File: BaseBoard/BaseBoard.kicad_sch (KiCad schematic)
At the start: 47 parts, among them J1 USB_C_DEALON-USB-US31-106, J2 Serial Port, J3 add-on conn, Q1 PMN48XP, SW1 SW_DIP_x08, SW2 boot, SW3 Reset, U1 ESP32-WROOM-E, U2 4021, U3 MCP73831-2ACI-OT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

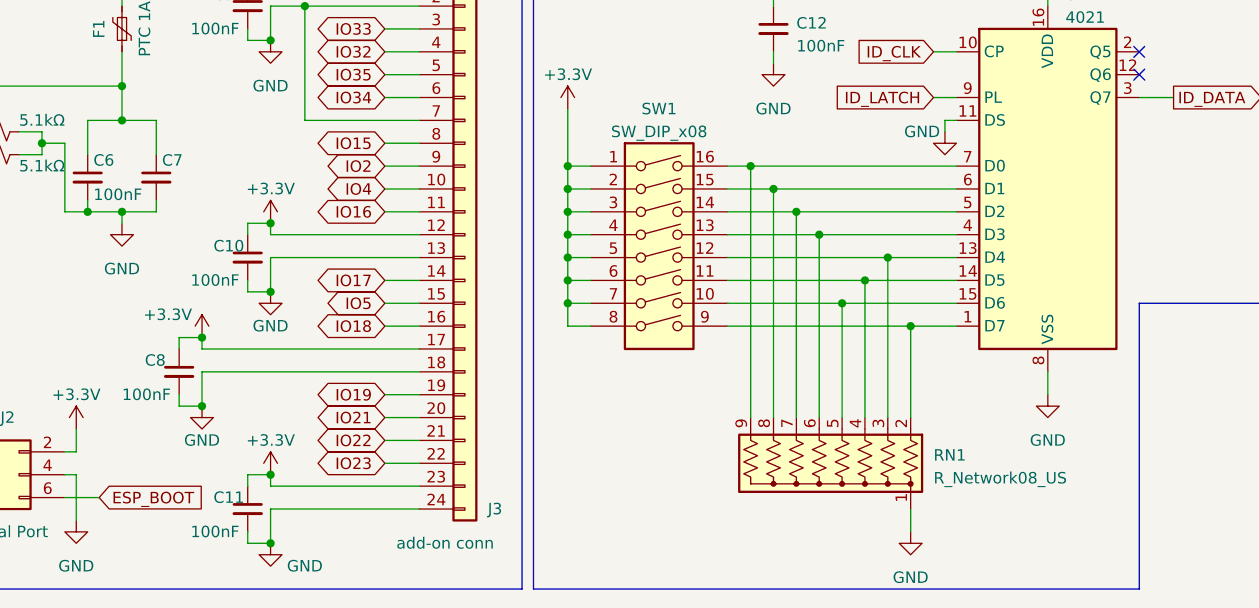
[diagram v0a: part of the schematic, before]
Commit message: Switches Resistor Network for actual footprint
We'll use the 746X101 which has a smaller footprint.
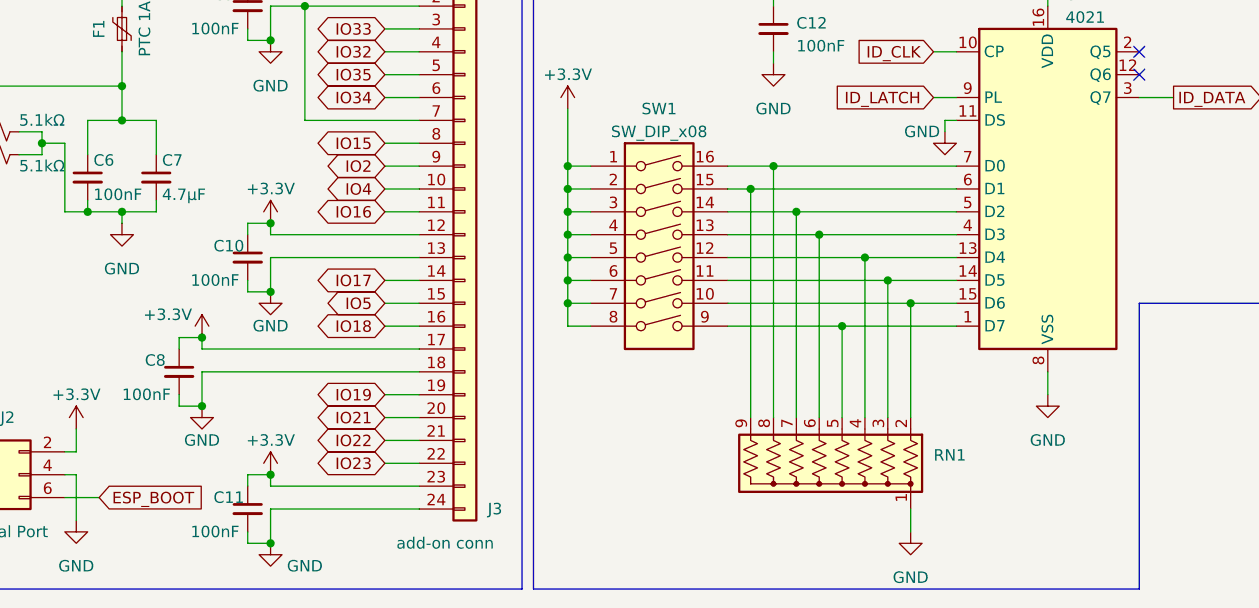
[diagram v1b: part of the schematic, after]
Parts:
- C7: value (none) -> 4.7µF
- RN1: value R_Network08_US -> (none); footprint Resistor_SMD:R_Array_Convex_5x1206 -> (none)
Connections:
- net at SW1.9, U2.1 (D7): now also RN1.5 (R4); no longer RN1.2 (R1)
- net at SW1.12, U2.13 (D4): now also RN1.4 (R3); no longer RN1.3 (R2)
- net at SW1.11, U2.14 (D5): now also RN1.3 (R2); no longer RN1.4 (R3)
- net at SW1.10, U2.15 (D6): now also RN1.2 (R1); no longer RN1.5 (R4)
- net at SW1.15, U2.6 (D1): now also RN1.9 (R8); no longer RN1.8 (R7)
- net at SW1.16, U2.7 (D0): now also RN1.8 (R7); no longer RN1.9 (R8)

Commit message: Moves symbol and footprint libraries to parent directory
This will allow us to use the symbols and footprints on other boards.
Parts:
- J3: value add-on conn -> (none)
- RN1: value (none) -> 10kΩ

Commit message: Fixes RGB led symbol
The Hongzhi Forest HS-1204-RGB is actually a BGAR led. Pin 1 is blue, 2
is green, 3 is the anode and 4 is red. The old symbol had red and the
anode swapped, which means the LED doesn't work correctly in rev 0.1 of
the board.
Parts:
- removed D2: LED_RGBA, GameOver:Hongzhi_Forest_HS-1204-RGB, symbol Device:LED_RGBA
- added D2: LED_BGAR, symbol Device:LED_BGAR
- J3: value (none) -> base connector
- RN1: footprint (none) -> GameOver:746X101
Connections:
- net +3V3: now also D2.3 (A)
- net at R12.2: now also D2.1 (BK)
- net at R10.2: now also D2.4 (RK)
- net at R11.2: now also D2.2 (GK)
